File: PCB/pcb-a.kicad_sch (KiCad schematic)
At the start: 29 parts, among them Q1 BC327, Q3 BC337, SW1 config, U1 MCP23008-xP, U2 MAX232I, U4 ATmega16L-8P, Y1 8Mhz

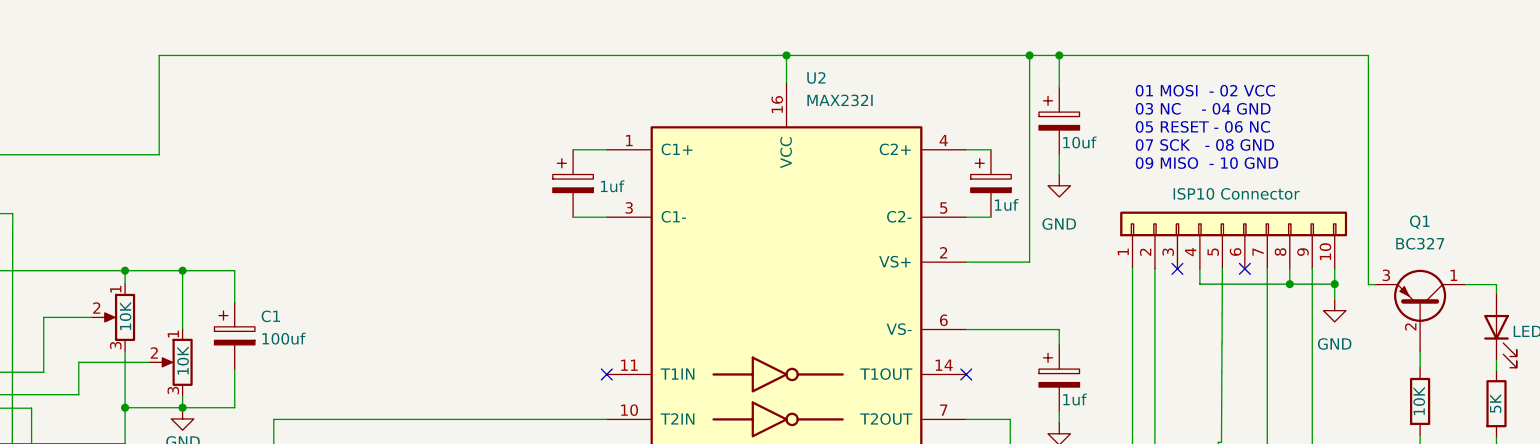
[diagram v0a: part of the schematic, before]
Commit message: 20 Ohm resistor added for MAX232
I got overheating experience on that chip. So, I looked for some info on internet. But I found just a post that suggest to add
the resistor to prevent capacitor dircharge trouble. I have tried the solution and it looks like function very well. But don't
ask me why!!! :-(
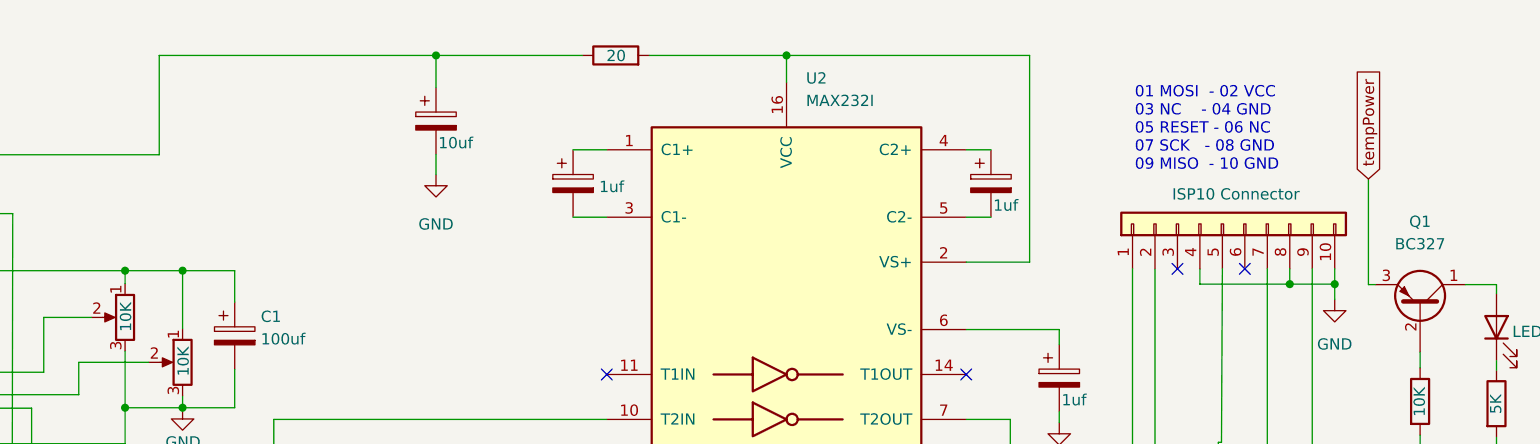
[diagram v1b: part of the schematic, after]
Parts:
- added R11: 20, Resistor_THT:R_Axial_DIN0204_L3.6mm_D1.6mm_P5.08mm_Horizontal, symbol Device:R
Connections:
- net tempPower: now also R11.1; no longer U2.16 (VCC), U2.2 (VS+)
- new net: R11.2, U2.16 (VCC), U2.2 (VS+)
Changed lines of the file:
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@@
 	)
 	(junction
-		(at 225.3488 19.304)
+		(at 104.8004 46.2788)
 		(diameter 0)
 		(color 0 0 0 0)
 	)
 	(junction
-		(at 104.8004 46.2788)
+		(at 158.242 19.304)
 		(diameter 0)
 		(color 0 0 0 0)
@@
 	)
 	(junction
-		(at 228.7016 19.304)
-		(diameter 0)
-		(color 0 0 0 0)
-	)
-	(junction
 		(at 59.0804 38.7604)
 		(diameter 0)
@@
 	(wire
 		(pts
-			(xy 126.9492 19.304) (xy 197.866 19.304)
+			(xy 126.9492 19.304) (xy 158.242 19.304)
 		)
 		(stroke
@@
 	(wire
 		(pts
-			(xy 228.7016 30.5308) (xy 228.7016 32.766)
+			(xy 158.242 30.5308) (xy 158.242 32.766)
 		)
 		(stroke
@@
 	(wire
 		(pts
+			(xy 182.372 19.304) (xy 197.866 19.304)
+		)
+		(stroke
+			(width 0)
+			(type default)
+		)
+	)
+	(wire
+		(pts
 			(xy 129.5908 57.8104) (xy 129.5908 59.1312)
 		)
@@
 	(wire
 		(pts
-			(xy 263.652 45.212) (xy 263.652 19.304)
-		)
-		(stroke
-			(width 0)
-			(type default)
-		)
-	)
-	(wire
-		(pts
 			(xy 74.3204 50.038) (xy 81.534 50.038)
 		)
@@
 	(wire
 		(pts
+			(xy 263.652 33.274) (xy 263.652 45.212)
+		)
+		(stroke
+			(width 0)
+			(type default)
+		)
+	)
+	(wire
+		(pts
 			(xy 129.5908 59.1312) (xy 123.0884 59.1312)
 		)
@@
 	(wire
 		(pts
+			(xy 158.242 19.304) (xy 174.752 19.304)
+		)
+		(stroke
+			(width 0)
+			(type default)
+		)
+	)
+	(wire
+		(pts
 			(xy 228.7016 50.292) (xy 228.7016 51.9684)
 		)
@@
 	(wire
 		(pts
-			(xy 225.3488 19.304) (xy 228.7016 19.304)
-		)
-		(stroke
-			(width 0)
-			(type default)
-		)
-	)
-	(wire
-		(pts
 			(xy 239.522 43.434) (xy 239.522 97.5868)
 		)
@@
 	(wire
 		(pts
-			(xy 228.7016 19.304) (xy 263.652 19.304)
-		)
-		(stroke
-			(width 0)
-			(type default)
-		)
-	)
-	(wire
-		(pts
 			(xy 94.4372 131.1148) (xy 94.4372 103.378)
 		)
@@
 	(wire
 		(pts
-			(xy 228.7016 22.9108) (xy 228.7016 19.304)
+			(xy 158.242 22.9108) (xy 158.242 19.304)
 		)
 		(stroke
@@
 		)
 	)
+	(global_label "tempPower"
+		(shape input)
+		(at 263.652 33.274 90)
+		(fields_autoplaced yes)
+		(effects
+			(font
+				(size 1.27 1.27)
+			)
+			(justify left)
+		)
+		(property "Intersheetrefs" "${INTERSHEET_REFS}"
+			(at 263.652 20.0079 90)
+			(effects
+				(font
+					(size 1.27 1.27)
+				)
+				(justify left)
+				(hide yes)
+			)
+		)
+		(property "Riferimenti inter-foglio" "${INTERSHEET_REFS}"
+			(at 265.8428 33.274 90)
+			(effects
+				(font
+					(size 1.27 1.27)
+				)
+				(justify left)
+				(hide yes)
+			)
+		)
+	)
 	(global_label "i_upLight"
 		(shape input)
@@
 	(symbol
 		(lib_id "Device:C_Polarized")
-		(at 228.7016 26.7208 0)
+		(at 158.242 26.7208 0)
 		(unit 1)
 		(exclude_from_sim no)
@@
 		(dnp no)
 		(property "Reference" "C7"
-			(at 231.648 24.5617 0)
+			(at 161.1884 24.5617 0)
 			(effects
 				(font
@@
 		)
 		(property "Value" "10uf"
-			(at 228.9556 29.21 0)
+			(at 158.496 29.21 0)
 			(effects
 				(font
@@
 		)
 		(property "Footprint" "Capacitor_THT:CP_Radial_D8.0mm_P2.50mm"
-			(at 229.6668 30.5308 0)
+			(at 159.2072 30.5308 0)
 			(effects
 				(font
@@
 		)
 		(property "Datasheet" "~"
-			(at 228.7016 26.7208 0)
+			(at 158.242 26.7208 0)
 			(effects
 				(font
@@
 		)
 		(property "Description" ""
-			(at 228.7016 26.7208 0)
+			(at 158.242 26.7208 0)
 			(effects
 				(font
@@
 	)
 	(symbol
+		(lib_id "Device:R")
+		(at 178.562 19.304 90)
+		(unit 1)
+		(exclude_from_sim no)
+		(in_bom yes)
+		(on_board yes)
+		(dnp no)
+		(property "Reference" "R11"
+			(at 178.562 13.6652 90)
+			(effects
+				(font
+					(size 1.27 1.27)
+				)
+				(hide yes)
+			)
+		)
+		(property "Value" "20"
+			(at 178.6128 19.3548 90)
+			(effects
+				(font
+					(size 1.27 1.27)
+				)
+			)
+		)
+		(property "Footprint" "Resistor_THT:R_Axial_DIN0204_L3.6mm_D1.6mm_P5.08mm_Horizontal"
+			(at 178.562 21.082 90)
+			(effects
+				(font
+					(size 1.27 1.27)
+				)
+				(hide yes)
+			)
+		)
+		(property "Datasheet" "~"
+			(at 178.562 19.304 0)
+			(effects
+				(font
+					(size 1.27 1.27)
+				)
+				(hide yes)
+			)
+		)
+		(property "Description" ""
+			(at 178.562 19.304 0)
+			(effects
+				(font
+					(size 1.27 1.27)
+				)
+				(hide yes)
+			)
+		)
+		(pin "1"
+		)
+		(pin "2"
+		)
+		(instances
+			(project "pcb-a"
+				(path "/709d0967-afe5-49d3-92a5-d2bb94550bdb"
+					(reference "R11")
+					(unit 1)
+				)
+			)
+		)
+	)
+	(symbol
 		(lib_id "Device:C_Polarized")
 		(at 135.4836 51.0032 0)
@@
 	(symbol
 		(lib_id "power:GND")
-		(at 228.7016 32.766 0)
+		(at 158.242 32.766 0)
 		(unit 1)
 		(exclude_from_sim no)
@@
 		(fields_autoplaced yes)
 		(property "Reference" "#PWR01"
-			(at 228.7016 39.116 0)
+			(at 158.242 39.116 0)
 			(effects
 				(font
@@
 		)
 		(property "Value" "GND"
-			(at 228.7016 38.4048 0)
+			(at 158.242 38.4048 0)
 			(effects
 				(font
@@
 		)
 		(property "Footprint" ""
-			(at 228.7016 32.766 0)
+			(at 158.242 32.766 0)
 			(effects
 				(font
@@
 		)
 		(property "Datasheet" ""
-			(at 228.7016 32.766 0)
+			(at 158.242 32.766 0)
 			(effects
 				(font
@@
 		)
 		(property "Description" ""
-			(at 228.7016 32.766 0)
+			(at 158.242 32.766 0)
 			(effects
 				(font

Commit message: Important comment added
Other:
- note added: "MAX 10K Ohm for ATmega16"
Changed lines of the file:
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@@
+		)
+	)
+	(text "MAX 10K Ohm for ATmega16"
+		(exclude_from_sim no)
+		(at 128.016 40.64 0)
+		(effects
+			(font
+				(size 1.27 1.27)
+			)
 		)
 	)

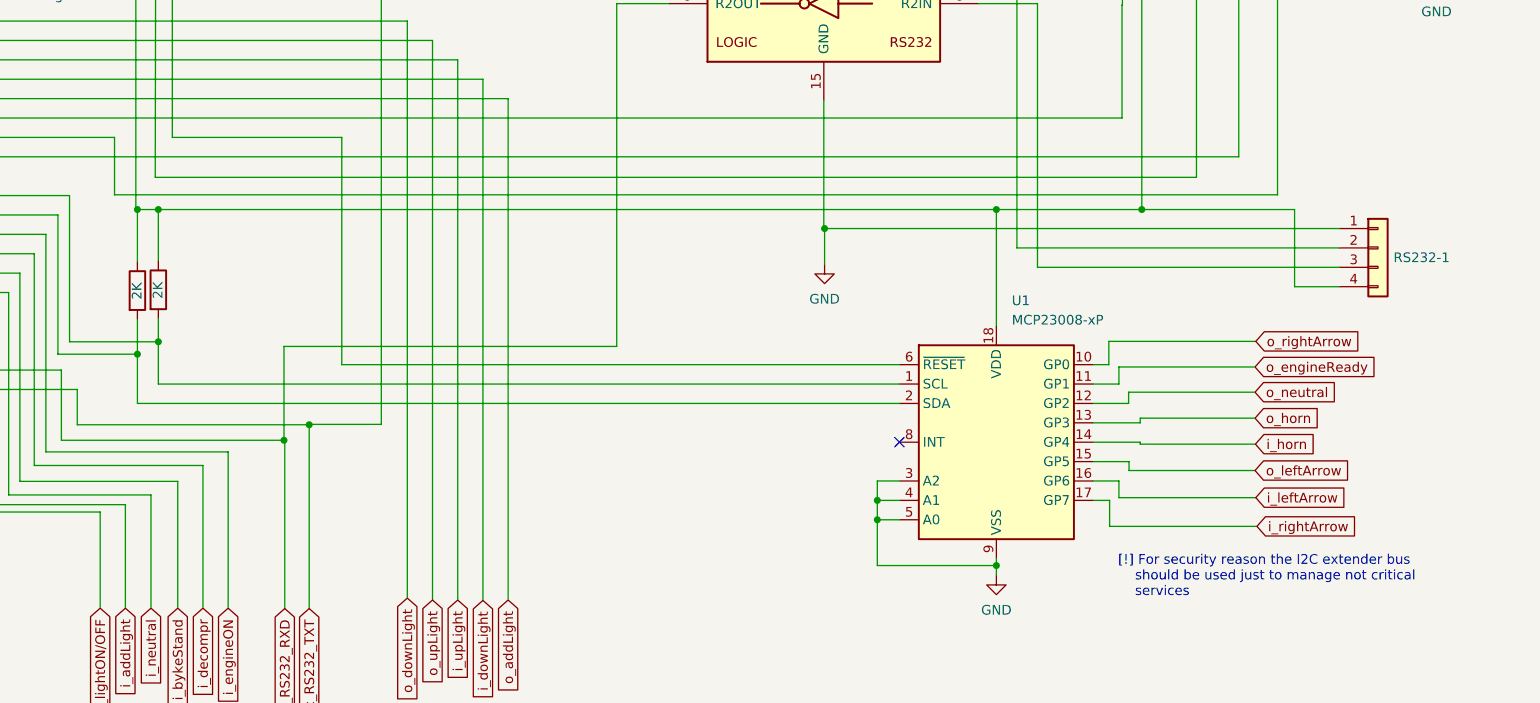
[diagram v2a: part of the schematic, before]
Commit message: Parking button added and Horn management removed
Horn is connected directly to the power PCB
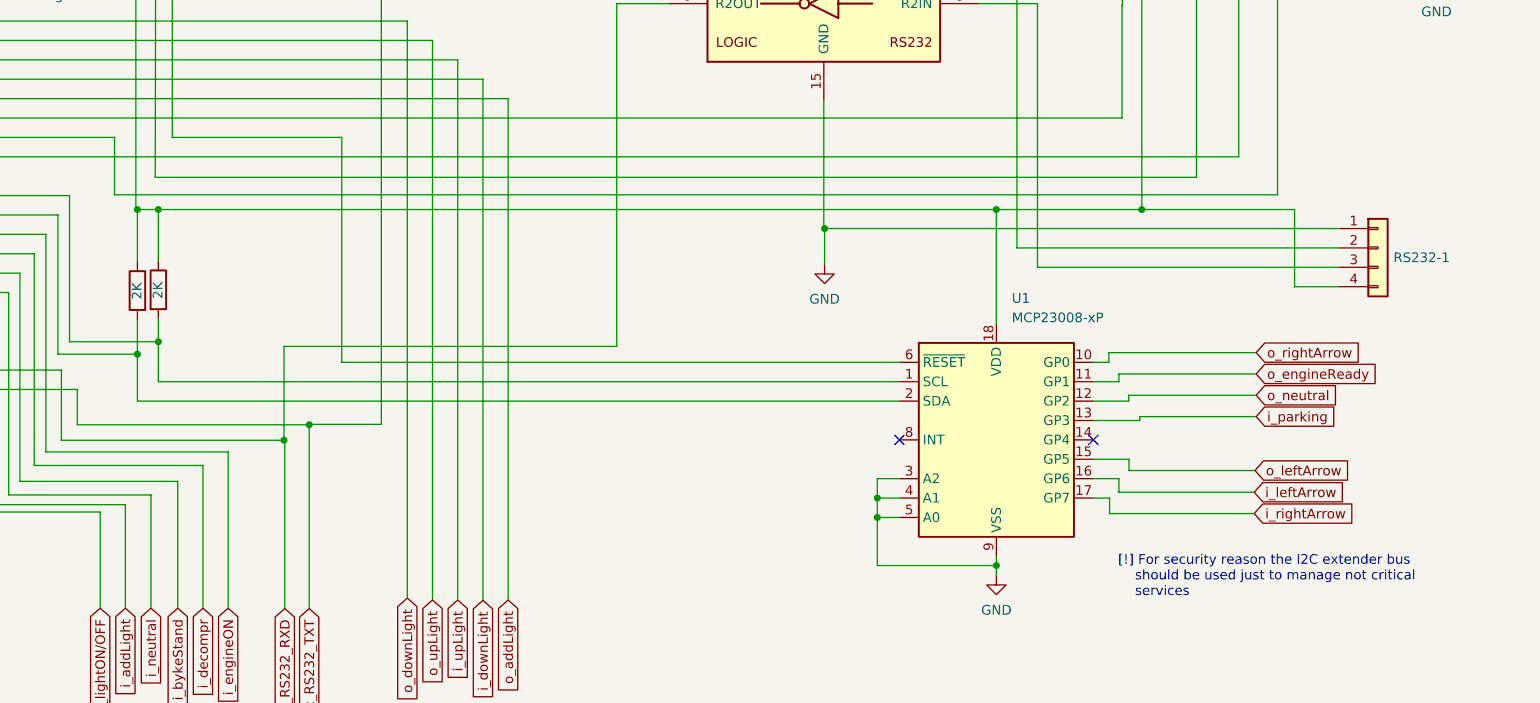
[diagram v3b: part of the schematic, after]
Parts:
- R10, R2, R3, R4, R5, R6, R7, R8, R9: footprint Resistor_THT:R_Axial_DIN0207_L6.3mm_D2.5mm_P7.62mm_Horizontal -> Resistor_THT:R_Axial_DIN0204_L3.6mm_D1.6mm_P5.08mm_Horizontal
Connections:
- net i_horn: no longer names the net of U1.14 (GP4)
- net o_horn renamed i_parking
- no-connect marks 10 -> 11

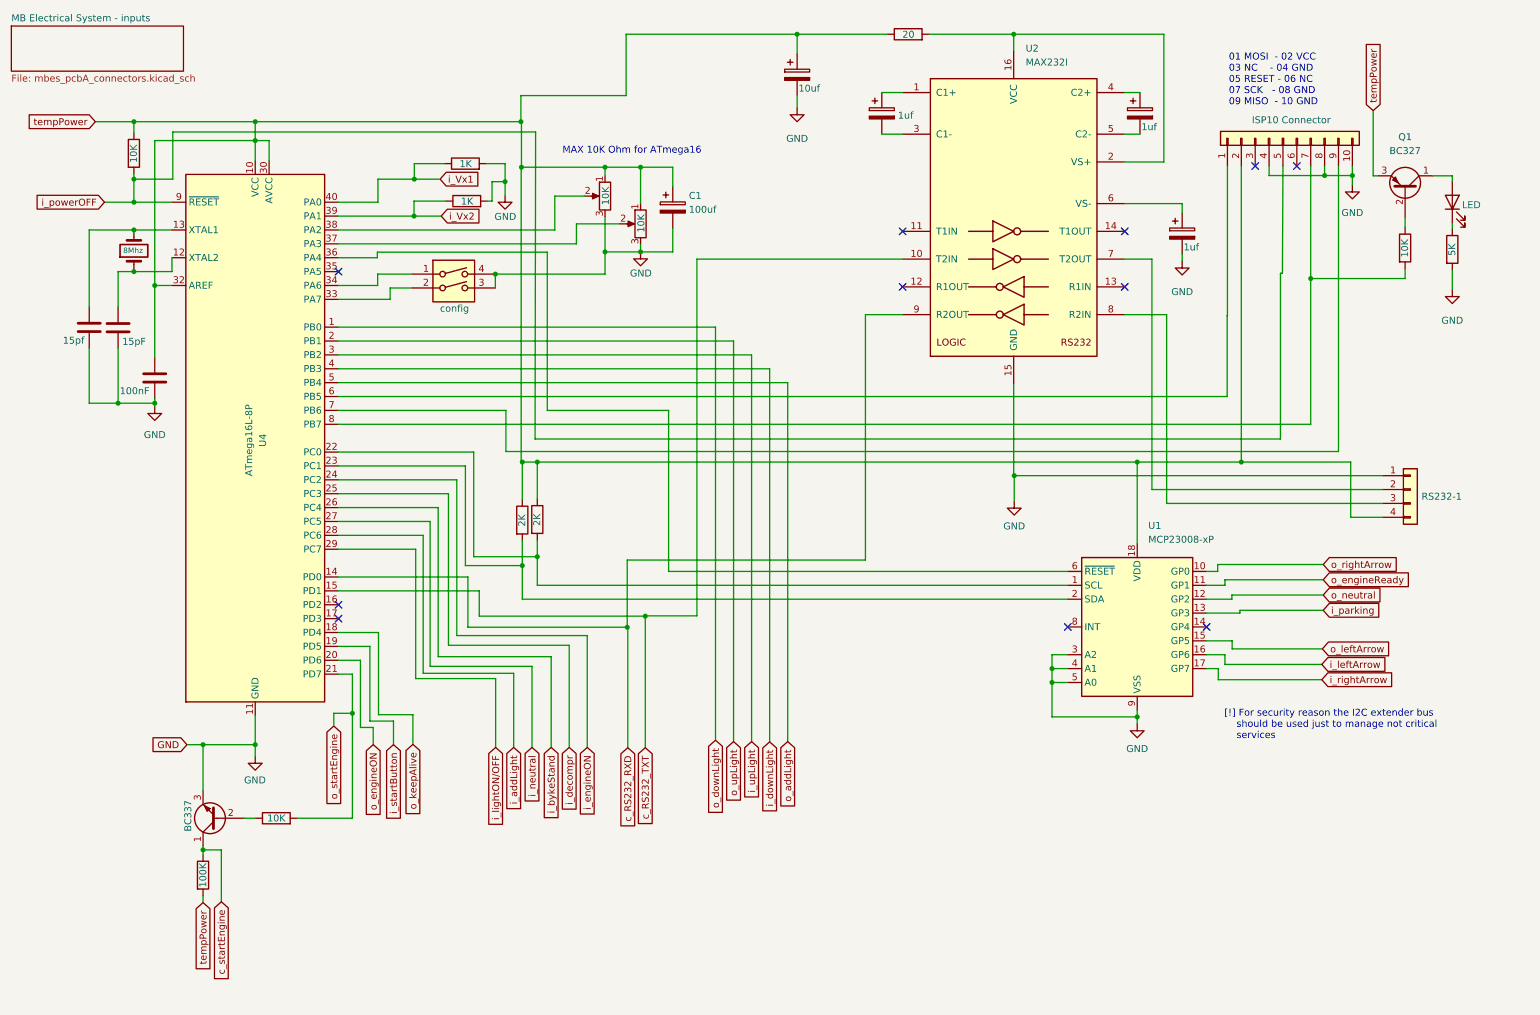
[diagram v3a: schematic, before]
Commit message: o_NEUTRAL is connected directly to the led
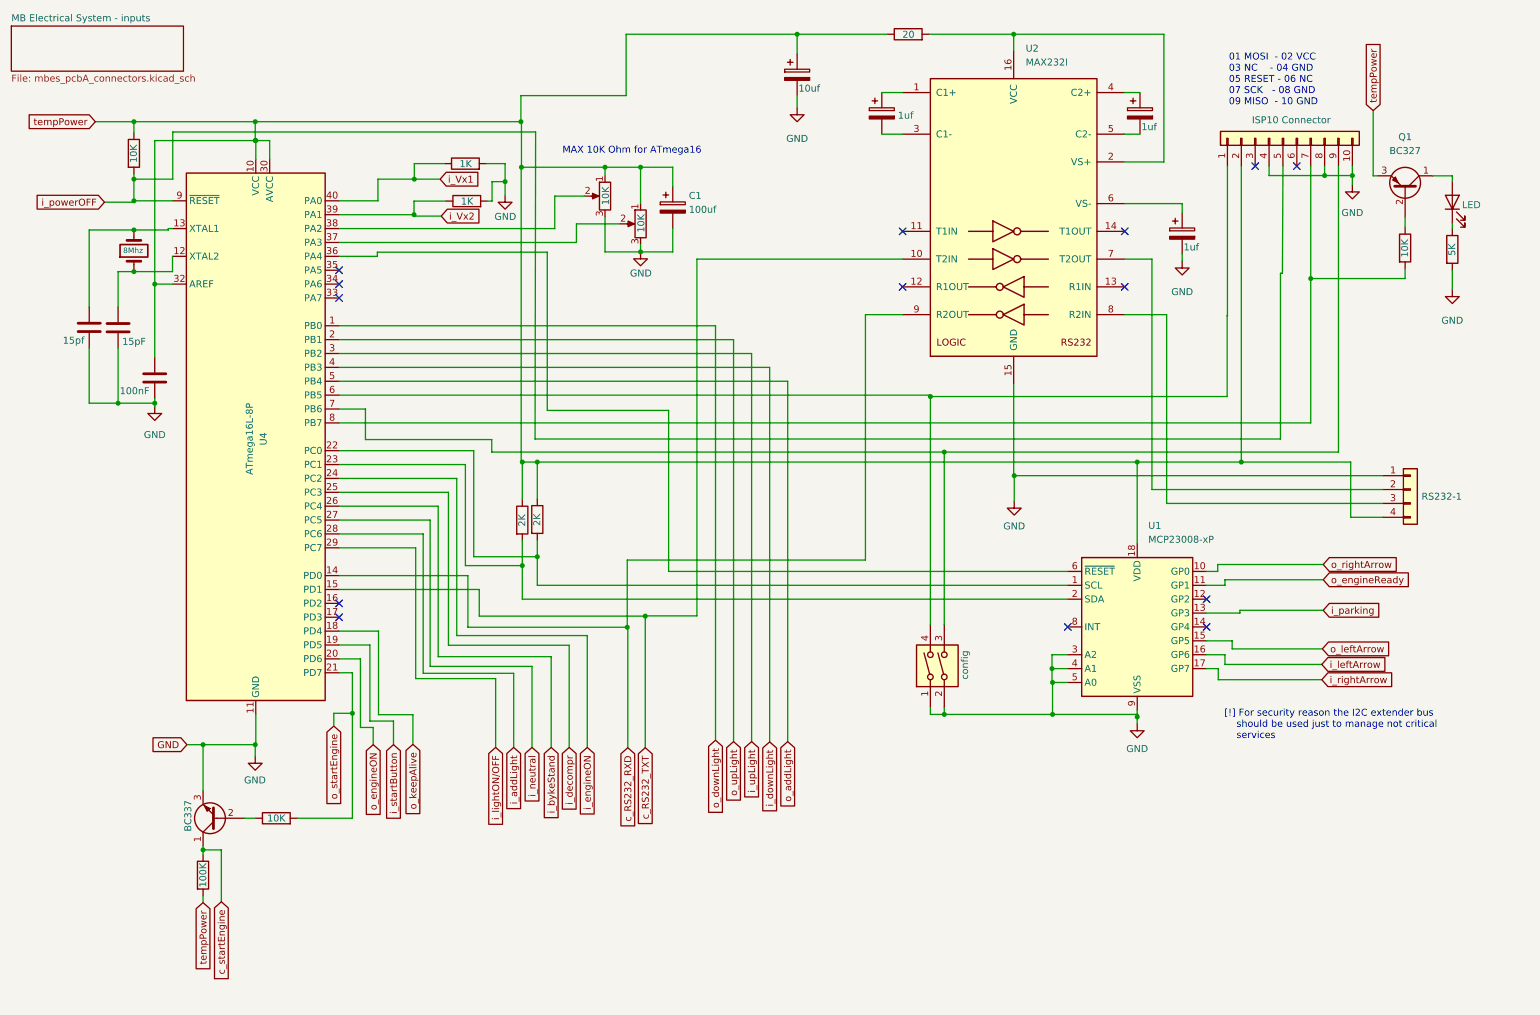
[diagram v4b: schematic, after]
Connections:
- net GND: now also SW1.1, SW1.2; no longer SW1.3, SW1.4
- net at U4.33 (PA7): no longer SW1.2
- net at U4.34 (PA6): no longer SW1.1
- net at ISP101.1 (Pin_1), U4.6 (PB5): now also SW1.4
- net at ISP101.9 (Pin_9), U4.7 (PB6): now also SW1.3
- net o_neutral: no longer names the net of U1.12 (GP2)
- no-connect marks 11 -> 14
